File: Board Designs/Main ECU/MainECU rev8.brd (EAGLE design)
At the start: 120.6 x 78.9 mm, 218 parts, among them J1 JUMPER, J2 JUMPER, J3 JUMPER, J4 JUMPER, J5 JUMPER, J6 JUMPER, J7 JUMPER, J8 JUMPER, P1 SOLDER_PAD, P2 SOLDER_PAD, Q1 P-CHANNEL_MOSFET_DMP3099L-7, Q12 P-CHANNEL_MOSFET_DMP3099L-7, X1 CONNECTOR-37, X2 CONNECTOR-4AUTOSPORT, X3 CONNECTOR-4NANO-FIT-VERTICAL-4, X4 CONNECTOR-4NANO-FIT-VERTICAL-4

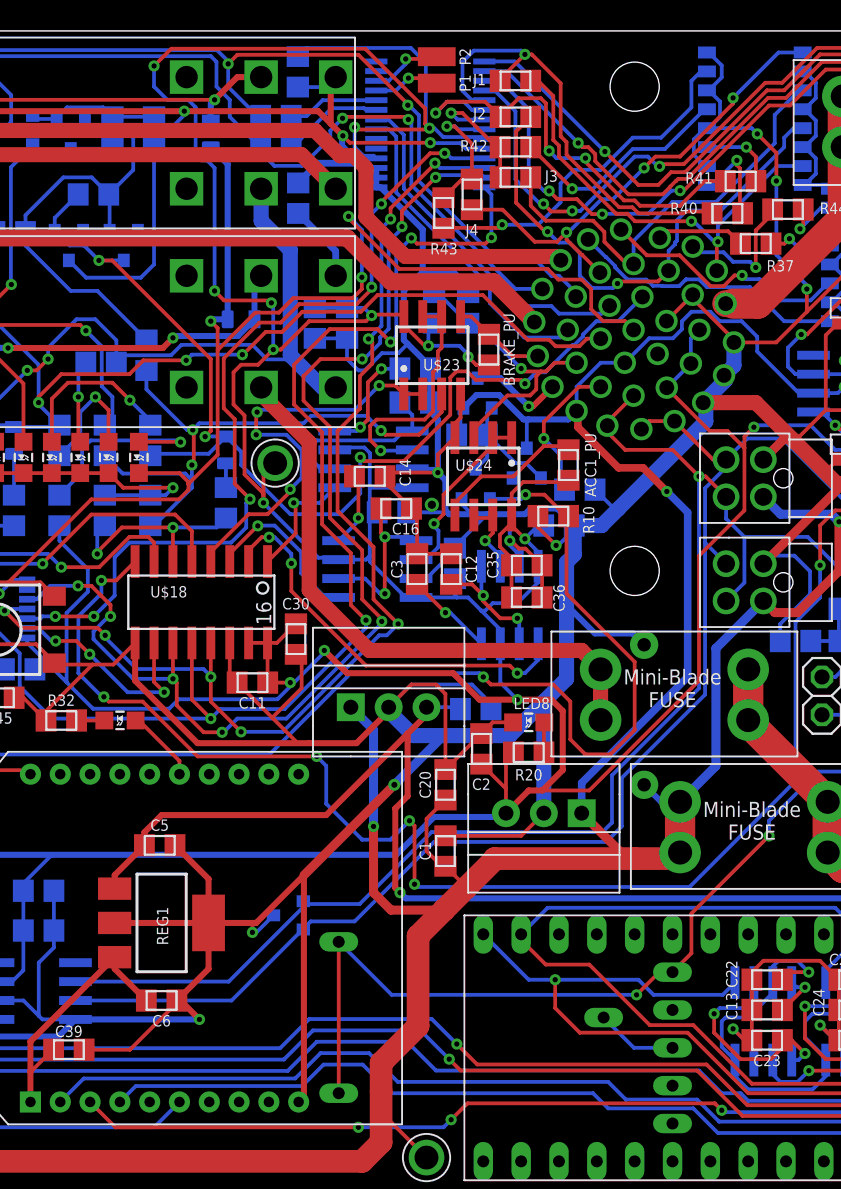
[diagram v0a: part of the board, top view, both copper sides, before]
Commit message: Manufactured versions of Main ECU rev7 and rev8
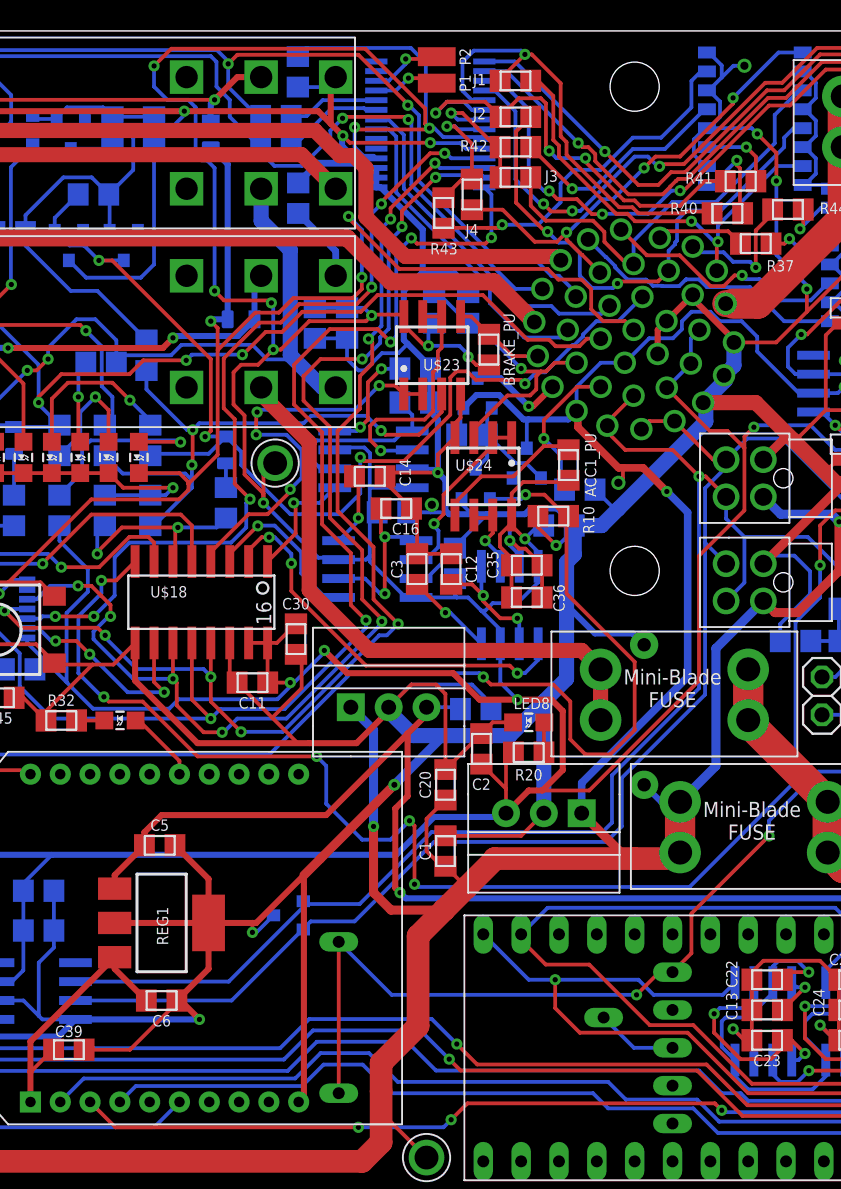
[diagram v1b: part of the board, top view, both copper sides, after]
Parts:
- C14, C17, C3: value 47nF -> 1nF
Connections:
- net GND: now also X1.P$35
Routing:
- net GND: track 987.7 -> 992.0 mm, vias 38 -> 39
- net +12V: track 433.1 -> 434.2 mm, vias 13 -> 14
- added copper zone on layer 2, net +12V
- added copper zone on layer 15, net GND
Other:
- board text added: "+12V"
- board text added: "HyTech 2019 Main ECU rev8"
- board text removed: "HyTech 2019 Main ECU rev7"
